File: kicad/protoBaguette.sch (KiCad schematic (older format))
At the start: 28 parts

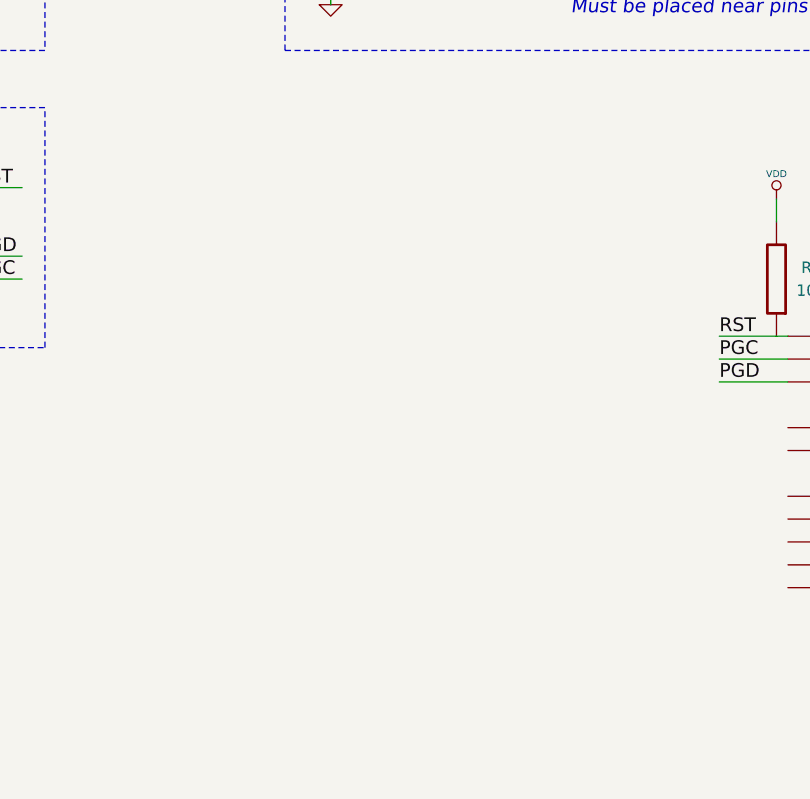
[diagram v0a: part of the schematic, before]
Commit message: Add PIC32MX150 schematic symbol
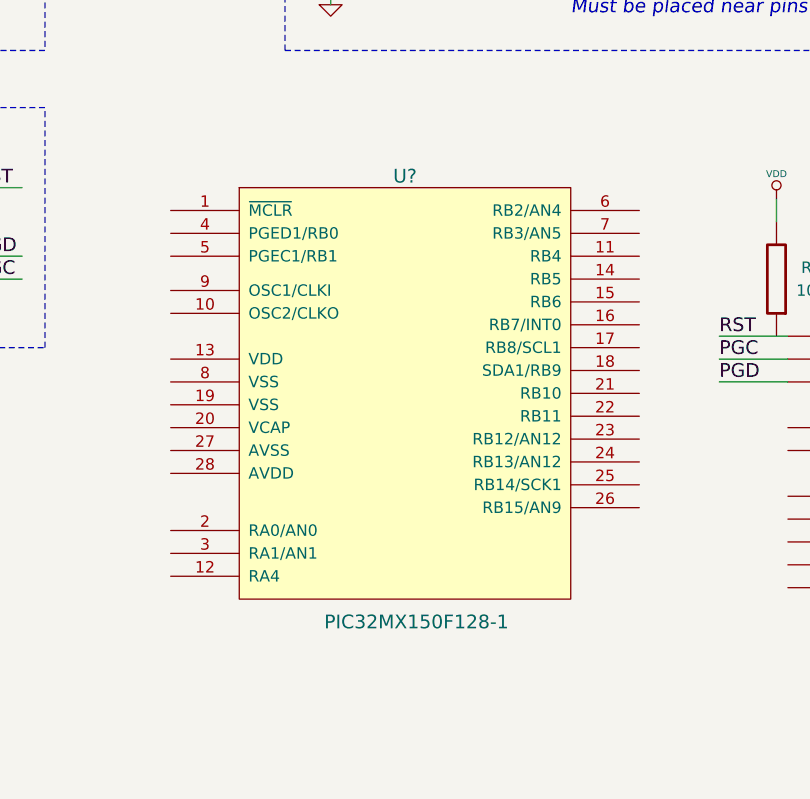
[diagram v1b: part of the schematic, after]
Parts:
- added U?: PIC32MX150F128-1, symbol PIC32MX150F128-1
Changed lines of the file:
@@
-EESchema Schematic File Version 2  date lun. 20 mai 2013 22:23:52 CEST
+EESchema Schematic File Version 2  date mer. 29 mai 2013 21:37:41 CEST
 LIBS:power
 LIBS:device
@@
 LIBS:protoBaguette
 LIBS:valves
+LIBS:protoBaguette-cache
 EELAYER 25  0
 EELAYER END
@@
 Sheet 1 1
 Title "Alpha prototype"
-Date "20 may 2013"
+Date "29 may 2013"
 Rev "0.1"
 Comp "ProtoBaguette"
@@
 $EndDescr
 $Comp
+L PIC32MX150F128-1 U?
+U 1 1 51A65900
+P 3400 2950
+F 0 "U?" H 3425 3650 60  0000 C CNN
+F 1 "PIC32MX150F128-1" H 3475 1700 60  0000 C CNN
+	1    3400 2950
+	1    0    0    -1
+$EndComp
+$Comp
 L R R?

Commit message: SCH
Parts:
- removed Cpll, Crx, Cvdd?: 100n, symbol C
- removed U?: PIC24F04KA201-PB-1, symbol PIC24F04KA201-PB-1
- added Cvcap: 100n?, symbol C
- added D?: LED, symbol LED
- added R?: R, symbol R
- renumbered Ctx to Cavdd, Cosc to Cosc?
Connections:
- net labels added: VCAP
- wire segments 81 -> 77
- no-connect marks 0 -> 3
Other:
- note removed: "To check"
- moved on the sheet: Cosc?, R?, U?
